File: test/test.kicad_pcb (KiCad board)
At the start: 2 copper layers, 19 x 12.7 mm, 1 part

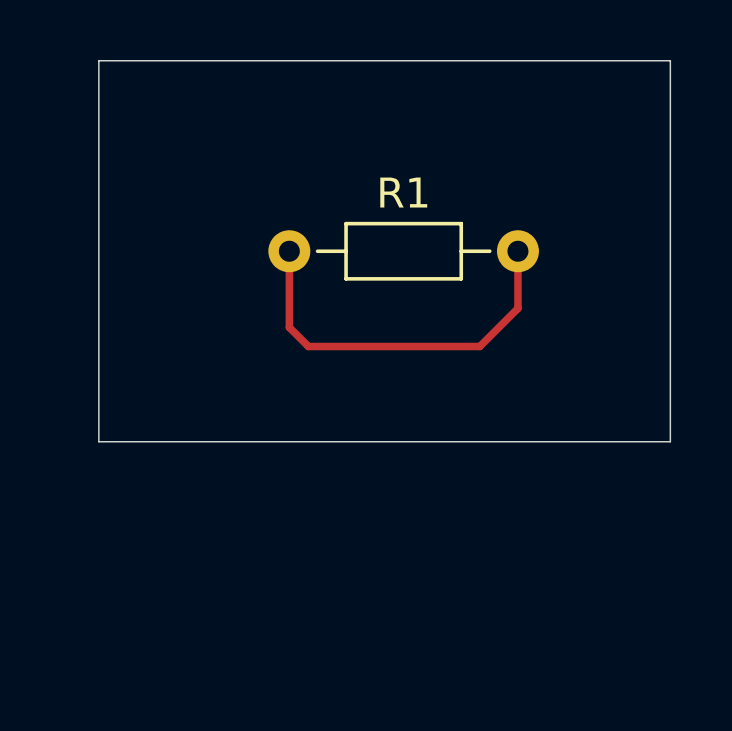
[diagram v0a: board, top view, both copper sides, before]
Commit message: improved test PCB
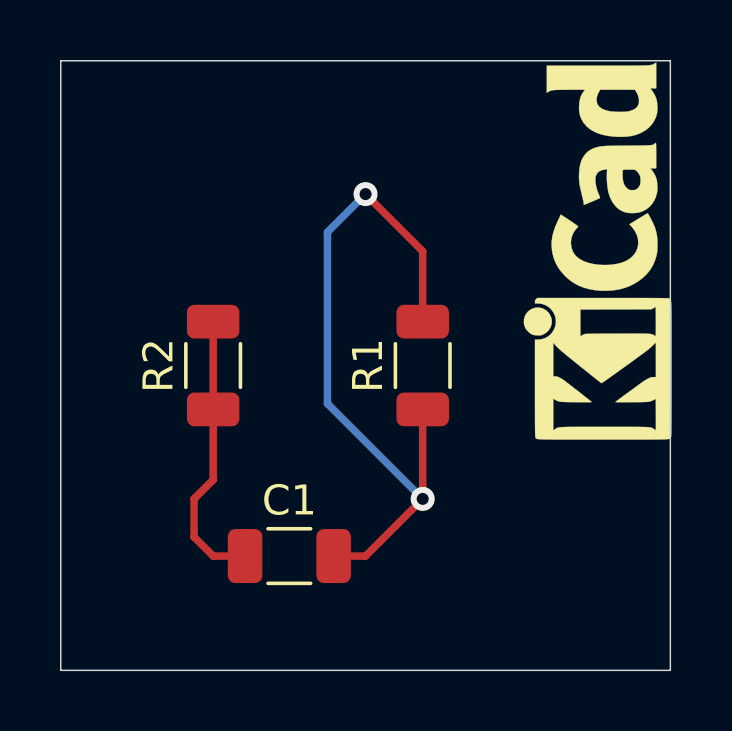
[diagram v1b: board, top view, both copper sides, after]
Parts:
- added C1: C, Capacitor_SMD:C_1206_3216Metric, F.Cu at (127.0, 105.4)
- added LOGO1: Logo_Open_Hardware_Large, Symbol:KiCad-Logo_5mm_SilkScreen, F.Cu at (137.8, 95.2)
- added R2: 100, Resistor_SMD:R_1206_3216Metric, F.Cu at (124.5, 99.1)
- R1: footprint Resistor_THT:R_Axial_DIN0204_L3.6mm_D1.6mm_P7.62mm_Horizontal -> Resistor_SMD:R_1206_3216Metric
- moved R1 5.85 mm to (131.4, 99.1), turned to 90 degrees
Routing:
- net Net-(C1-Pad2): track 12.9 -> 24.0 mm, vias 0 -> 2
- net Net-(C1-Pad1): track 0.00 -> 10.1 mm
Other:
- board size 19 x 12.7 mm -> 20.3 x 20.3 mm
